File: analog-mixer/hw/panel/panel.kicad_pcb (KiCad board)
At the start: 4 copper layers, 129 x 189 mm, 444 parts, among them J1 SJ-43514-SMT, J10 GCT USB4085, J11 Модуль IP2326: VBUS, GND, BAT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, J2 SJ-43514-SMT, J3 SJ-43514-SMT, J4 SJ-43514-SMT, J5 SJ-43514-SMT, J6 SJ-43514-SMT MAIN, J7 SJ-43514-SMT SEND, J8 SJ-43514-SMT PHONES, J9 PBS-24 до цифрової плати, Q1 AO3401A, SW1 CTS 204-121ST, SW10 Cherry MX, SW11 Cherry MX, SW12 MSK12C02 вимикач живлення, SW2 Cherry MX, SW3 CTS 204-121ST, SW4 Cherry MX, SW5 CTS 204-121ST, SW6 Cherry MX, SW7 CTS 204-121ST, SW8 Cherry MX, SW9 CTS 204-121ST, U1 OPA1678, U10 DG413, U11 OPA1678, U12 DG413, U13 OPA1678, U14 OPA1678, U15 OPA1678, U16 OPA1678, U17 OPA1678, U18 OPA1678, U19 TL064AC, U2 DG413, U20 TL064AC, U21 TL064AC, U22 TL064AC, U23 TL064AC, U24 TL064AC, U25 MCP23017-E/SO, U26 USBLC6-2SC6, U27 CH340N, U28 LT1930ES5, U29 LT1931ES5, U3 OPA1678, U30 TPS62933O, U4 DG413, U5 OPA1678, U6 DG413, U7 OPA1678, U8 DG413, U9 OPA1678

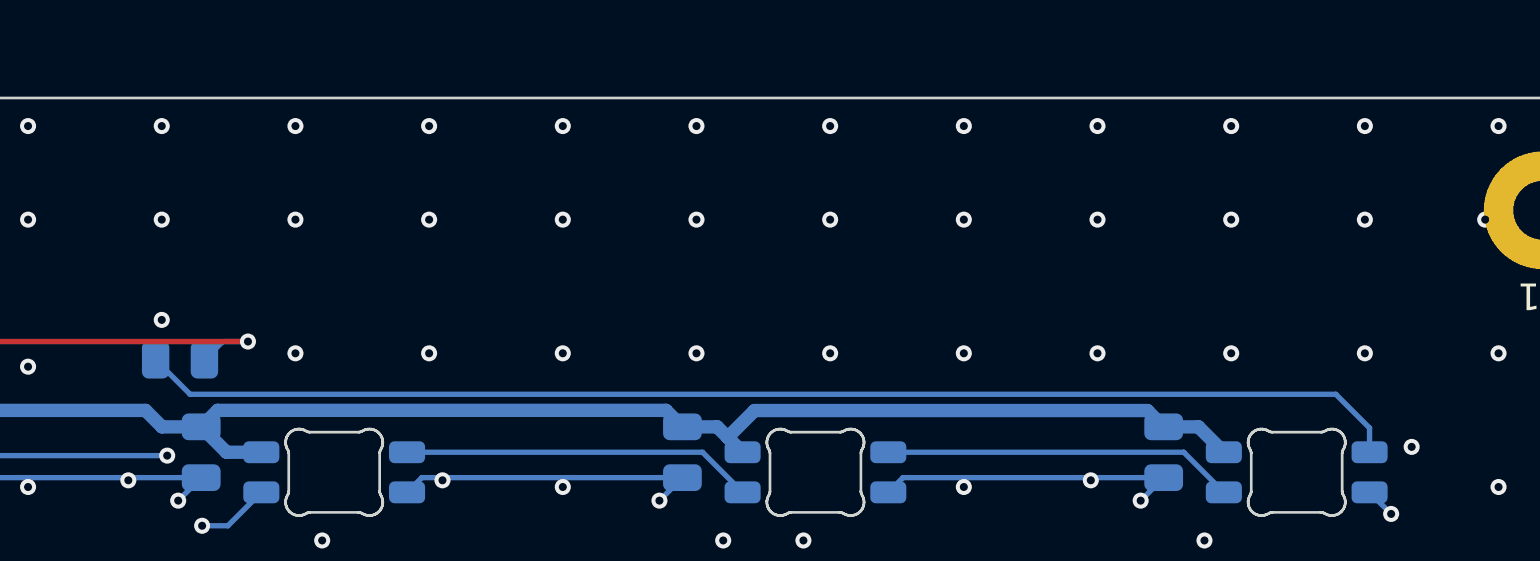
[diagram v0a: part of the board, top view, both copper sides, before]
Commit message: Адреса джерел на шовкографії обох плат (D9, CERN-OHL-S розд. 4)
- build_pcb.ATTRIB / add_attribution(), hw/pcb/add_silk.py для розведених плат
- panel.py: файл правил DRC — за іменем файлу (шлях analog-mixer/ ламав відбір)
- панель і hw/fab перезібрано; DRC: 0 розривів, нових зауважень немає

Co-Authored-By: Claude Opus 5.5 <noreply@anthropic.com>
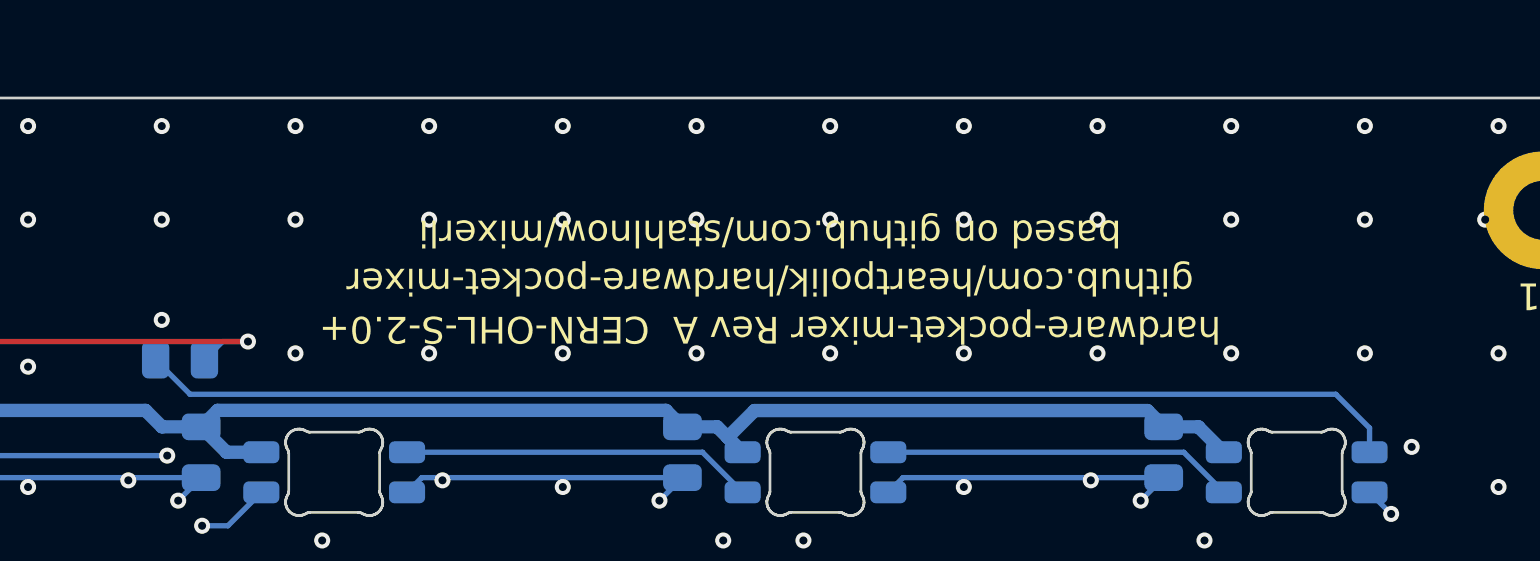
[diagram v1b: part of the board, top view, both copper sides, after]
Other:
- board text added: "based on github.com/stahlnow/mixerli"
- board text added: "github.com/heartpolik/hardware-pocket-mixer"
- board text added: "hardware-pocket-mixer Rev A CERN-OHL-S-2.0+"
